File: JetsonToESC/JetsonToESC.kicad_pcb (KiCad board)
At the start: 2 copper layers, 70 x 50 mm, 47 parts, among them J1 Conn_01x12, J2 Conn_01x02, J3 Conn_01x02, J4 Screw_Terminal_01x01, J5 Screw_Terminal_01x01, U1 ESP32-C3_SUPERMINI_TH, U2 DS18B20, U3 LMR51420XDDCR, U4 MCP23018x-x-SS, U5 ACS759ECB-200B-PFF-T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

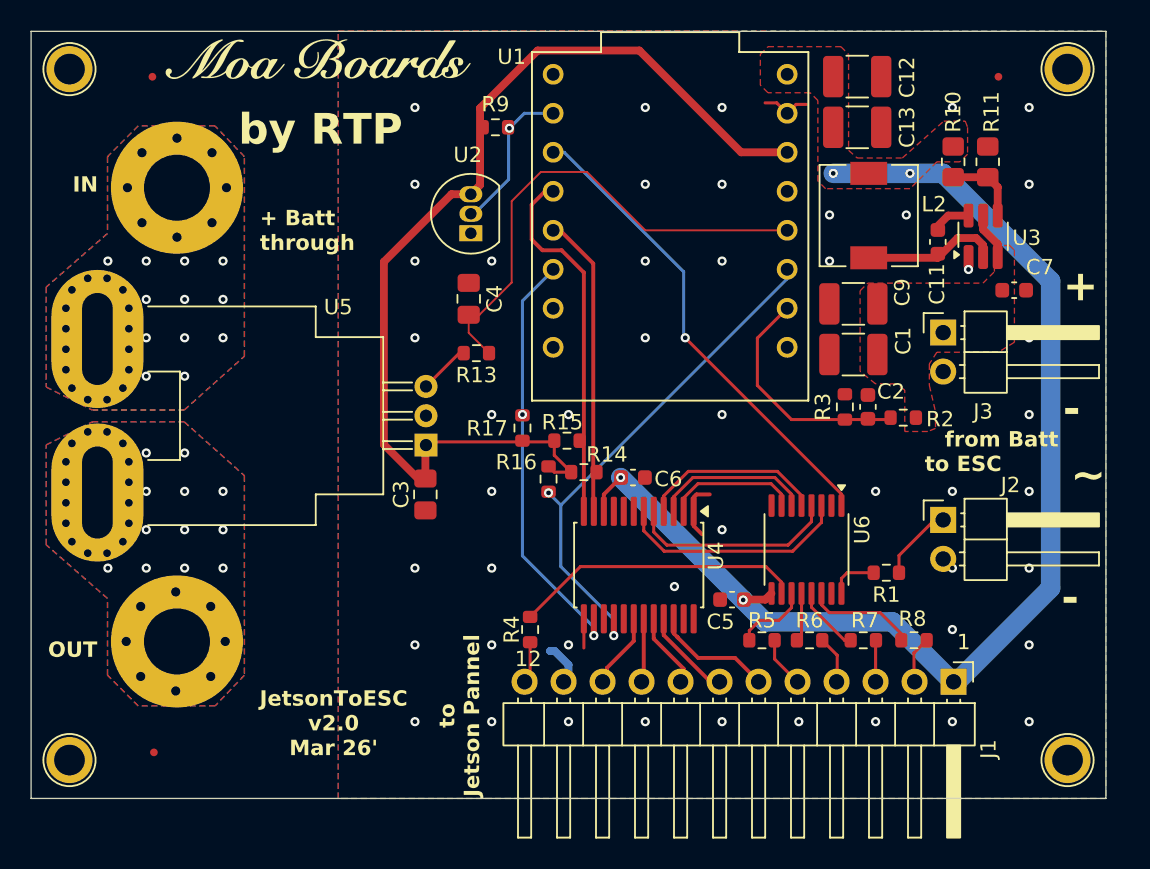
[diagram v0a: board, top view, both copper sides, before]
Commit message: Changed connectors to headers and routed
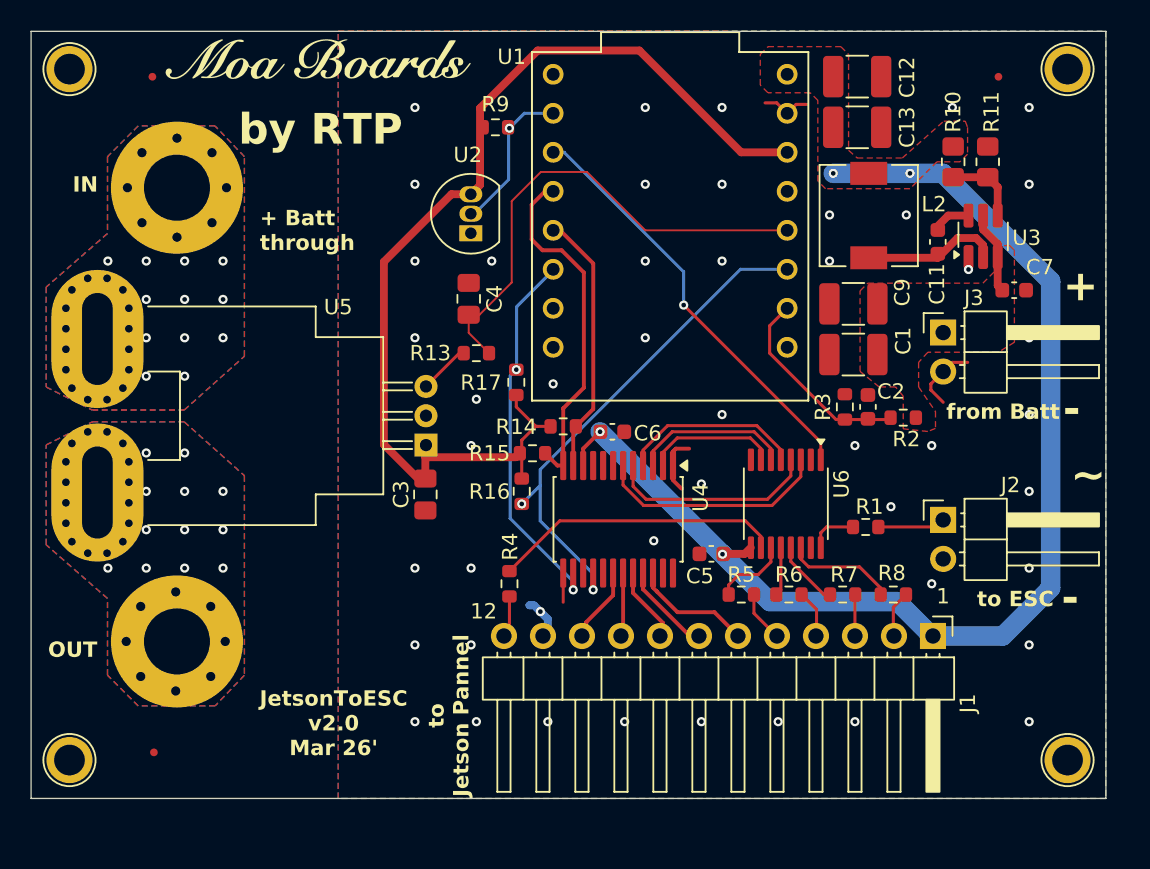
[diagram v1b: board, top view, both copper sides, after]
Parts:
- moved C5 3.27 mm to (154.3, 114.1)
- moved J1 3.27 mm to (168.7, 119.4)
- moved R1 3.27 mm to (164.4, 112.3)
- moved R14 3.27 mm to (144.7, 105.8)
- moved R4 3.27 mm to (141.2, 116.0)
- moved R5 3.27 mm to (156.3, 116.7)
- moved R6 3.27 mm to (159.4, 116.7)
- moved R7 3.27 mm to (162.9, 116.7)
- moved R8 3.27 mm to (166.2, 116.7)
- moved U4 3.27 mm to (148.2, 111.8)
- moved C6 3.27 mm to (147.9, 106.1)
- moved U6 3.27 mm to (159.2, 110.8)
- moved R17 3.00 mm to (141.6, 102.9)
- moved R15 2.39 mm to (142.7, 107.5)
- moved R16 1.92 mm to (142.0, 110.0)
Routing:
- net GND: track 12.4 -> 17.8 mm
- net PWM: track 31.2 -> 27.7 mm
- net I2C_RESET: track 28.0 -> 25.1 mm
- net 3V3: track 66.9 -> 69.4 mm
- net I2C_SCL: track 19.7 -> 17.3 mm
- net BATT_LEVEL_SENSE: track 15.5 -> 13.1 mm
- net VBAT: track 3.09 -> 5.38 mm
- net I2C_SDA: track 23.9 -> 23.0 mm
- net ESC_PWM: track 4.98 -> 4.41 mm

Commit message: Edit mounting holes to 3mm
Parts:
- H1, H2, H3, H4: footprint TestPoint:TestPoint_Plated_Hole_D2.0mm -> TestPoint:TestPoint_Plated_Hole_D3.0mm
- moved H2 1.75 mm to (176.6, 84.0)
- moved H3 1.68 mm to (113.4, 126.1)
- moved H1 1.53 mm to (113.4, 83.7)
- moved H4 1.47 mm to (176.7, 126.3)
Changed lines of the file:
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@@
 		)
 	)
-	(footprint "TestPoint:TestPoint_Plated_Hole_D2.0mm"
+	(footprint "TestPoint:TestPoint_Plated_Hole_D3.0mm"
 		(layer "F.Cu")
-		(at 177.5 82.5)
-		(descr "Plated Hole as test Point, diameter 2.0mm")
+		(at 176.606062 84.00408)
+		(descr "Plated Hole as test Point, diameter 3.0mm")
 		(tags "test point plated hole")
 		(property "Reference" "H2"
-			(at 0 -2.498 0)
+			(at 0 -3.048 0)
 			(layer "F.SilkS")
 			(hide yes)
@@
 		)
 		(property "Value" "MountingHole"
-			(at 0 2.45 0)
+			(at 0 3 0)
 			(layer "F.Fab")
 			(hide yes)
@@
 		(fp_circle
 			(center 0 0)
-			(end 0 -1.7)
+			(end 0 -2.286)
 			(stroke
 				(width 0.12)
@@
 		(fp_circle
 			(center 0 0)
-			(end 1.8 0)
+			(end 2.5 0)
 			(stroke
 				(width 0.05)
@@
 			(fill no)
 			(layer "F.CrtYd")
+		)
+		(fp_text user "${REFERENCE}"
+			(at 0 -3.05 0)
+			(layer "F.Fab")
+			(effects
+				(font
+					(size 1 1)
+					(thickness 0.15)
+				)
+			)
 		)
 		(pad "1" thru_hole circle
 			(at 0 0)
-			(size 3 3)
-			(drill 2)
+			(size 4 4)
+			(drill 3)
 			(layers "*.Cu" "*.Mask")
 			(remove_unused_layers no)
@@
 		)
 	)
-	(footprint "TestPoint:TestPoint_Plated_Hole_D2.0mm"
+	(footprint "TestPoint:TestPoint_Plated_Hole_D3.0mm"
 		(layer "F.Cu")
-		(at 177.5 127.5)
-		(descr "Plated Hole as test Point, diameter 2.0mm")
+		(at 176.708016 126.256004)
+		(descr "Plated Hole as test Point, diameter 3.0mm")
 		(tags "test point plated hole")
 		(property "Reference" "H4"
-			(at 0 -2.498 0)
+			(at 0 -3.048 0)
 			(layer "F.SilkS")
 			(hide yes)
@@
 		)
 		(property "Value" "MountingHole"
-			(at 0 2.45 0)
+			(at 0 3 0)
 			(layer "F.Fab")
 			(hide yes)
@@
 		(fp_circle
 			(center 0 0)
-			(end 0 -1.7)
+			(end 0 -2.286)
 			(stroke
 				(width 0.12)
@@
 		(fp_circle
 			(center 0 0)
-			(end 1.8 0)
+			(end 2.5 0)
 			(stroke
 				(width 0.05)
@@
 		)
 		(fp_text user "${REFERENCE}"
-			(at 0 -2.5 0)
+			(at 0 -3.05 0)
 			(layer "F.Fab")
 			(effects
@@
 		(pad "1" thru_hole circle
 			(at 0 0)
-			(size 3 3)
-			(drill 2)
+			(size 4 4)
+			(drill 3)
 			(layers "*.Cu" "*.Mask")
 			(remove_unused_layers no)
@@
 		)
 	)
-	(footprint "TestPoint:TestPoint_Plated_Hole_D2.0mm"
+	(footprint "TestPoint:TestPoint_Plated_Hole_D3.0mm"
 		(layer "F.Cu")
-		(at 112.5 82.5)
-		(descr "Plated Hole as test Point, diameter 2.0mm")
+		(at 113.435268 83.716934)
+		(descr "Plated Hole as test Point, diameter 3.0mm")
 		(tags "test point plated hole")
 		(property "Reference" "H1"
-			(at 0 -2.498 0)
+			(at 0 -3.048 0)
 			(layer "F.SilkS")
 			(hide yes)
@@
 		)
 		(property "Value" "MountingHole"
-			(at 0 2.45 0)
-			(layer "F.Fab")
-			(hide yes)
+			(at 0 3 0)
+			(layer "F.Fab")
 			(effects
 				(font
@@
 		(fp_circle
 			(center 0 0)
-			(end 0 -1.7)
+			(end 0 -2.286)
 			(stroke
 				(width 0.12)
@@
 		(fp_circle
 			(center 0 0)
-			(end 1.8 0)
+			(end 2.5 0)
 			(stroke
 				(width 0.05)
@@
 			(fill no)
 			(layer "F.CrtYd")
+		)
+		(fp_text user "${REFERENCE}"
+			(at 0 -3.05 0)
+			(layer "F.Fab")
+			(effects
+				(font
+					(size 1 1)
+					(thickness 0.15)
+				)
+			)
 		)
 		(pad "1" thru_hole circle
 			(at 0 0)
-			(size 3 3)
-			(drill 2)
+			(size 4 4)
+			(drill 3)
 			(layers "*.Cu" "*.Mask")
 			(remove_unused_layers no)
@@
 		(embedded_fonts no)
 	)
-	(footprint "TestPoint:TestPoint_Plated_Hole_D2.0mm"
+	(footprint "TestPoint:TestPoint_Plated_Hole_D3.0mm"
 		(layer "F.Cu")
-		(at 112.5 127.5)
-		(descr "Plated Hole as test Point, diameter 2.0mm")
+		(at 113.398492 126.083472)
+		(descr "Plated Hole as test Point, diameter 3.0mm")
 		(tags "test point plated hole")
 		(property "Reference" "H3"
-			(at 0 -2.498 0)
+			(at 0 -3.048 0)
 			(layer "F.SilkS")
 			(hide yes)
@@
 		)
 		(property "Value" "MountingHole"
-			(at 0 2.45 0)
+			(at 0 3 0)
 			(layer "F.Fab")
 			(hide yes)
@@
 		(fp_circle
 			(center 0 0)
-			(end 0 -1.7)
+			(end 0 -2.286)
 			(stroke
 				(width 0.12)
@@
 		(fp_circle
 			(center 0 0)
-			(end 1.8 0)
+			(end 2.5 0)
 			(stroke
 				(width 0.05)
@@
 		)
 		(fp_text user "${REFERENCE}"
-			(at 0 -2.5 0)
+			(at 0 -3.05 0)
 			(layer "F.Fab")
 			(effects
@@
 		(pad "1" thru_hole circle
 			(at 0 0)
-			(size 3 3)
-			(drill 2)
+			(size 4 4)
+			(drill 3)
 			(layers "*.Cu" "*.Mask")
 			(remove_unused_layers no)

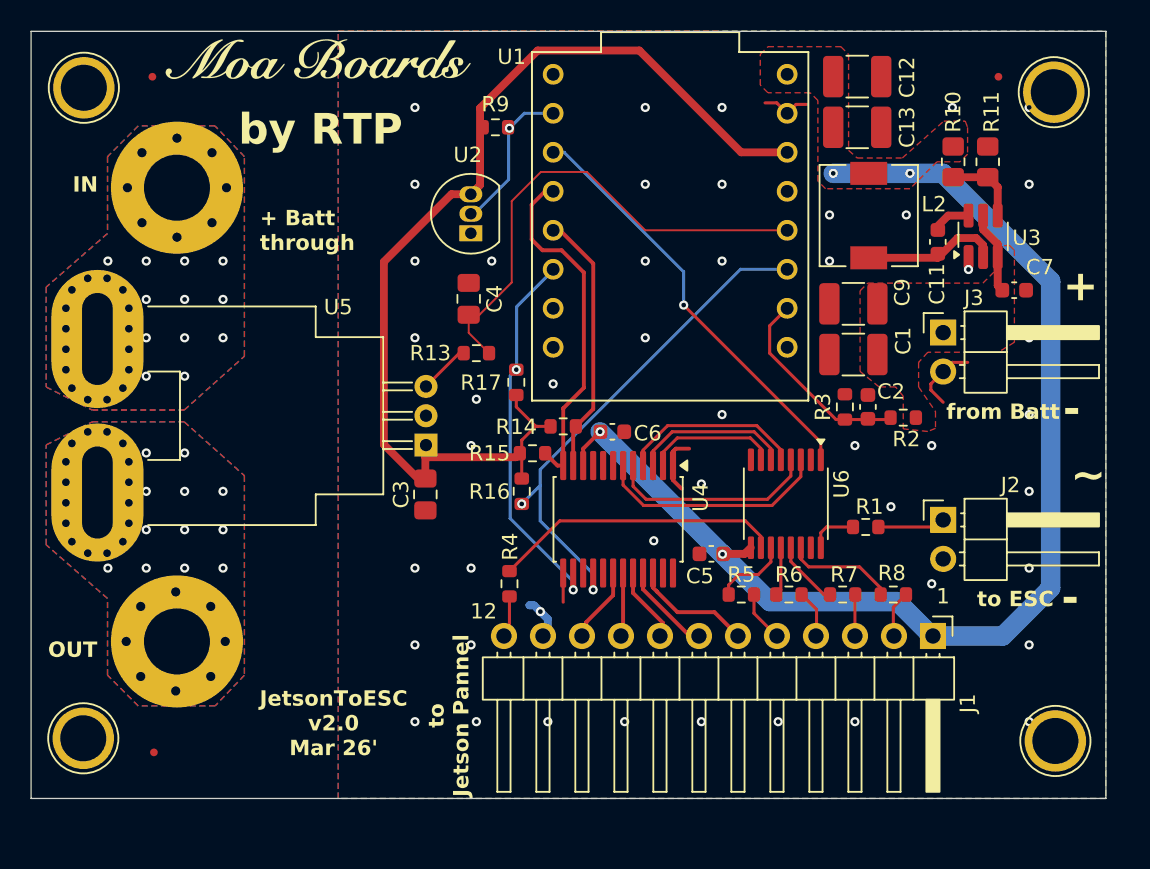
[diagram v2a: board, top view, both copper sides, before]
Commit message: Changed connectors into moles microfit
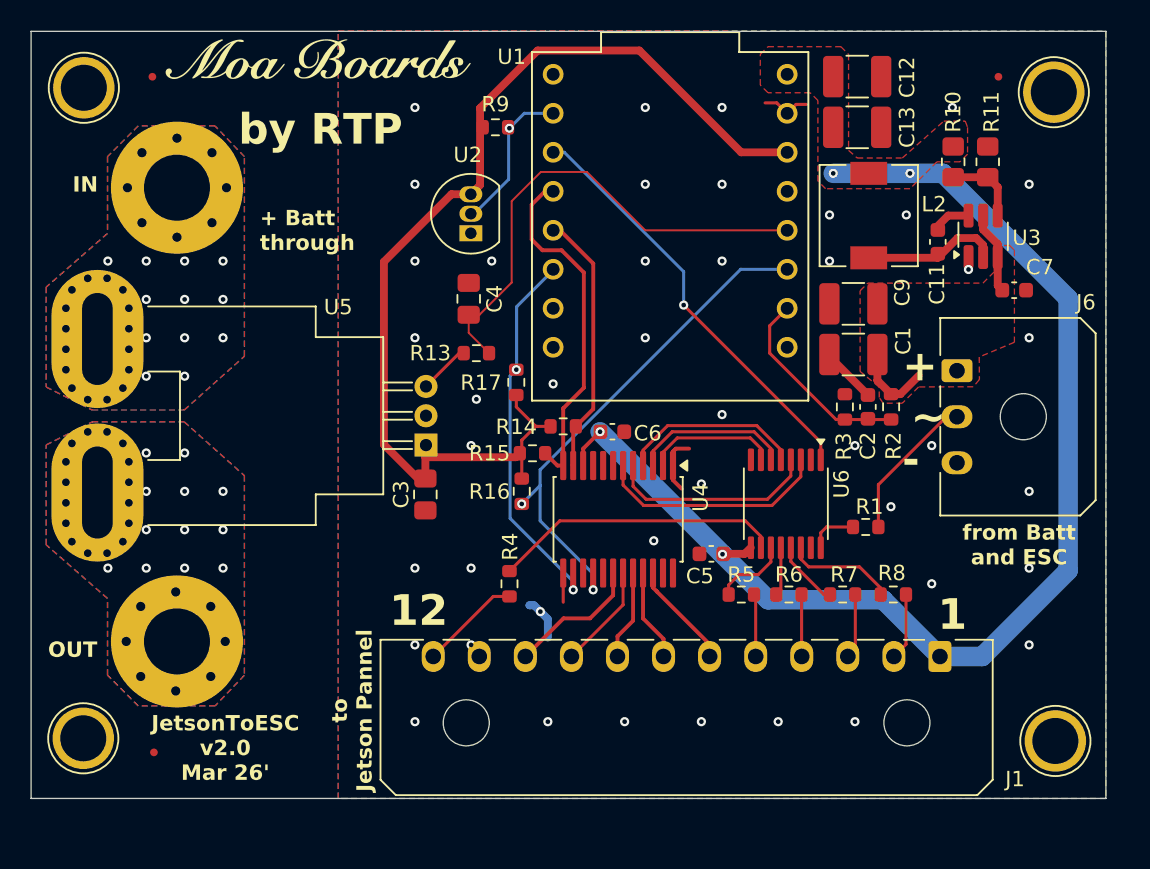
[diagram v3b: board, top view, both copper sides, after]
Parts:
- removed J2, J3: Conn_01x02, Connector_PinHeader_2.54mm:PinHeader_1x02_P2.54mm_Horizontal
- added J6: Conn_01x03, Connector_Molex:Molex_Micro-Fit_3.0_43650-0300_1x03_P3.00mm_Horizontal, F.Cu at (170.3, 102.1)
- J1: footprint Connector_PinHeader_2.54mm:PinHeader_1x12_P2.54mm_Horizontal -> Connector_Molex:Molex_Micro-Fit_3.0_43650-1200_1x12_P3.00mm_Horizontal
- moved J1 1.41 mm to (169.2, 120.8), turned to 180 degrees
- moved R2 1.06 mm to (166.0, 104.5), turned to -90 degrees
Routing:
- net ESC_PWM: track 4.41 -> 9.70 mm
- net VBAT: track 5.38 -> 10.6 mm
- net LED_TEMP: track 2.67 -> 6.58 mm
- net BUTTON_STOP: track 4.92 -> 8.82 mm
- net BUTTON_25%: track 4.24 -> 6.83 mm
- net 5V: track 78.0 -> 79.9 mm
- net GND: track 17.8 -> 16.1 mm, vias 48 -> 43
- net LED_BATT_MED: track 2.67 -> 4.24 mm
- net LED_BATT_LOW: track 3.14 -> 4.36 mm
- net BUTTON_100%: track 7.95 -> 6.96 mm
- net BUTTON_50%: track 5.01 -> 5.86 mm
- net LED_BATT_HI: track 3.22 -> 4.04 mm
- net LED_OVERCURRENT: track 3.45 -> 4.08 mm
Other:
- board text added: "from Batt and ESC"
- board text removed: "from Batt"
- board text removed: "to ESC"
